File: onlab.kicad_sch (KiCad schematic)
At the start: 82 parts, among them J1 Battery, J10 DC-Motor, J2 HC_SR04, J3 HC_SR04, J4 HC_SR04, J5 DC-Motor, J6 DC-Motor, J7 DC-Motor, J8 DC-Motor, J9 DC-Motor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

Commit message: Routing
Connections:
- net Mot2_DrvA: now also U5.13 (P12/GPIO12/ADC2_CH5); no longer U5.25 (P0/GPIO0/ADC2_CH1)
- net Mot2_DrvB: now also U5.15 (P13/GPIO13/ADC2_CH4); no longer U5.24 (P2/GPIO2/ADC_CH2)
- net Mot3_DrvA: now also U5.25 (P0/GPIO0/ADC2_CH1); no longer U5.13 (P12/GPIO12/ADC2_CH5)
- net Mot3_DrvB: now also U5.24 (P2/GPIO2/ADC_CH2); no longer U5.15 (P13/GPIO13/ADC2_CH4)
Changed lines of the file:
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@@
     (effects (font (size 1.27 1.27)) (justify right bottom))
   )
-  (label "Mot2_DrvA" (at 254 69.85 0) (fields_autoplaced)
+  (label "Mot3_DrvA" (at 254 69.85 0) (fields_autoplaced)
     (effects (font (size 1.27 1.27)) (justify left bottom))
   )
@@
     (effects (font (size 1.27 1.27)) (justify left bottom))
   )
-  (label "Mot2_DrvB" (at 254 72.39 0) (fields_autoplaced)
+  (label "Mot3_DrvB" (at 254 72.39 0) (fields_autoplaced)
     (effects (font (size 1.27 1.27)) (justify left bottom))
   )
@@
     (effects (font (size 1.27 1.27)) (justify left bottom))
   )
-  (label "Mot3_DrvA" (at 190.5 67.31 180) (fields_autoplaced)
+  (label "Mot2_DrvA" (at 190.5 67.31 180) (fields_autoplaced)
     (effects (font (size 1.27 1.27)) (justify right bottom))
   )
@@
     (effects (font (size 1.27 1.27)) (justify left bottom))
   )
-  (label "Mot3_DrvB" (at 190.5 72.39 180) (fields_autoplaced)
+  (label "Mot2_DrvB" (at 190.5 72.39 180) (fields_autoplaced)
     (effects (font (size 1.27 1.27)) (justify right bottom))
   )

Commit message: Routing part 2
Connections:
- net Mot1_DrvA: now also U5.10 (P26/GPIO26/ADC2_CH9); no longer U5.9 (P25/GPIO25/ADC2_CH8)
- net Mot1_DrvB: now also U5.9 (P25/GPIO25/ADC2_CH8); no longer U5.10 (P26/GPIO26/ADC2_CH9)
- net Mot1_EncA: now also U5.3 (SVP/GPIO36/ADC1_CH0); no longer U5.5 (P34/GPIO34/ADC1_CH6)
- net Mot1_EncB: now also U5.4 (SVN/GPIO39/ADC1_CH3); no longer U5.6 (P35/GPIO35/ADC1_CH7)
- net Mot2_DrvA: now also U5.8 (P33/GPIO33/ADC1_CH5); no longer U5.13 (P12/GPIO12/ADC2_CH5)
- net Mot2_DrvB: now also U5.7 (P32/GPIO32/ADC1_CH4); no longer U5.15 (P13/GPIO13/ADC2_CH4)
- net Mot2_EncA: now also U5.5 (P34/GPIO34/ADC1_CH6); no longer U5.7 (P32/GPIO32/ADC1_CH4)
- net Mot2_EncB: now also U5.6 (P35/GPIO35/ADC1_CH7); no longer U5.8 (P33/GPIO33/ADC1_CH5)
- net Mot3_EncA: now also U5.13 (P12/GPIO12/ADC2_CH5); no longer U5.3 (SVP/GPIO36/ADC1_CH0)
- net Mot3_EncB: now also U5.15 (P13/GPIO13/ADC2_CH4); no longer U5.4 (SVN/GPIO39/ADC1_CH3)
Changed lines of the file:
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@@
+    (effects (font (size 1.27 1.27)) (justify right bottom))
+  )
+  (label "Mot2_EncB" (at 190.5 49.53 180) (fields_autoplaced)
     (effects (font (size 1.27 1.27)) (justify right bottom))
   )
@@
     (effects (font (size 1.27 1.27)) (justify left bottom))
   )
+  (label "Mot1_EncB" (at 190.5 44.45 180) (fields_autoplaced)
+    (effects (font (size 1.27 1.27)) (justify right bottom))
+  )
   (label "UV_Trig_1" (at 44.45 248.92 180) (fields_autoplaced)
     (effects (font (size 1.27 1.27)) (justify right bottom))
@@
     (effects (font (size 1.27 1.27)) (justify right bottom))
   )
-  (label "Mot3_EncA" (at 190.5 41.91 180) (fields_autoplaced)
+  (label "Mot2_EncA" (at 190.5 46.99 180) (fields_autoplaced)
+    (effects (font (size 1.27 1.27)) (justify right bottom))
+  )
+  (label "Mot2_DrvB" (at 190.5 52.07 180) (fields_autoplaced)
     (effects (font (size 1.27 1.27)) (justify right bottom))
   )
@@
     (effects (font (size 1.27 1.27)) (justify right bottom))
   )
+  (label "Mot3_EncA" (at 190.5 67.31 180) (fields_autoplaced)
+    (effects (font (size 1.27 1.27)) (justify right bottom))
+  )
   (label "Mot3_A" (at 369.062 72.644 0) (fields_autoplaced)
     (effects (font (size 1.27 1.27)) (justify left bottom))
@@
     (effects (font (size 1.27 1.27)) (justify right bottom))
   )
+  (label "Mot1_DrvB" (at 190.5 57.15 180) (fields_autoplaced)
+    (effects (font (size 1.27 1.27)) (justify right bottom))
+  )
   (label "Mot2_DrvA" (at 351.282 49.784 180) (fields_autoplaced)
     (effects (font (size 1.27 1.27)) (justify right bottom))
@@
     (effects (font (size 1.27 1.27)) (justify right bottom))
   )
+  (label "Mot3_EncB" (at 190.5 72.39 180) (fields_autoplaced)
+    (effects (font (size 1.27 1.27)) (justify right bottom))
+  )
+  (label "Mot1_DrvA" (at 190.5 59.69 180) (fields_autoplaced)
+    (effects (font (size 1.27 1.27)) (justify right bottom))
+  )
   (label "Mot3_EncA" (at 352.425 234.95 180) (fields_autoplaced)
     (effects (font (size 1.27 1.27)) (justify right bottom))
@@
     (effects (font (size 1.27 1.27)) (justify left bottom))
   )
-  (label "Mot3_EncB" (at 190.5 44.45 180) (fields_autoplaced)
-    (effects (font (size 1.27 1.27)) (justify right bottom))
-  )
   (label "Mot3_A" (at 352.425 229.87 180) (fields_autoplaced)
     (effects (font (size 1.27 1.27)) (justify right bottom))
@@
     (effects (font (size 1.27 1.27)) (justify left bottom))
   )
+  (label "Mot2_DrvA" (at 190.5 54.61 180) (fields_autoplaced)
+    (effects (font (size 1.27 1.27)) (justify right bottom))
+  )
   (label "Mot1_EncB" (at 349.885 140.97 180) (fields_autoplaced)
     (effects (font (size 1.27 1.27)) (justify right bottom))
@@
     (effects (font (size 1.27 1.27)) (justify left bottom))
   )
-  (label "Mot2_EncB" (at 190.5 54.61 180) (fields_autoplaced)
-    (effects (font (size 1.27 1.27)) (justify right bottom))
-  )
   (label "Mot1_DrvB" (at 351.282 42.164 180) (fields_autoplaced)
     (effects (font (size 1.27 1.27)) (justify right bottom))
@@
     (effects (font (size 1.27 1.27)) (justify left bottom))
   )
-  (label "Mot2_DrvA" (at 190.5 67.31 180) (fields_autoplaced)
-    (effects (font (size 1.27 1.27)) (justify right bottom))
-  )
   (label "SCLK" (at 106.426 82.296 0) (fields_autoplaced)
     (effects (font (size 1.27 1.27)) (justify left bottom))
@@
     (effects (font (size 1.27 1.27)) (justify left bottom))
   )
-  (label "Mot2_DrvB" (at 190.5 72.39 180) (fields_autoplaced)
-    (effects (font (size 1.27 1.27)) (justify right bottom))
-  )
-  (label "Mot1_EncB" (at 190.5 49.53 180) (fields_autoplaced)
-    (effects (font (size 1.27 1.27)) (justify right bottom))
-  )
   (label "MPU95 interrupt" (at 266.954 83.312 0) (fields_autoplaced)
     (effects (font (size 1.27 1.27)) (justify left bottom))
@@
     (effects (font (size 1.27 1.27)) (justify left bottom))
   )
-  (label "Mot1_DrvA" (at 190.5 57.15 180) (fields_autoplaced)
-    (effects (font (size 1.27 1.27)) (justify right bottom))
-  )
   (label "Button_2" (at 207.01 129.54 180) (fields_autoplaced)
     (effects (font (size 1.27 1.27)) (justify right bottom))
@@
     (effects (font (size 1.27 1.27)) (justify left bottom))
   )
-  (label "Mot1_EncA" (at 190.5 46.99 180) (fields_autoplaced)
-    (effects (font (size 1.27 1.27)) (justify right bottom))
-  )
   (label "Mot2_DrvB" (at 351.282 52.324 180) (fields_autoplaced)
     (effects (font (size 1.27 1.27)) (justify right bottom))
@@
     (effects (font (size 1.27 1.27)) (justify right bottom))
   )
+  (label "Mot1_EncA" (at 190.5 41.91 180) (fields_autoplaced)
+    (effects (font (size 1.27 1.27)) (justify right bottom))
+  )
   (label "I2C_SDA" (at 42.418 136.398 180) (fields_autoplaced)
     (effects (font (size 1.27 1.27)) (justify right bottom))
@@
     (effects (font (size 1.27 1.27)) (justify right bottom))
   )
-  (label "Mot1_DrvB" (at 190.5 59.69 180) (fields_autoplaced)
-    (effects (font (size 1.27 1.27)) (justify right bottom))
-  )
   (label "nCS" (at 254 59.69 0) (fields_autoplaced)
     (effects (font (size 1.27 1.27)) (justify left bottom))
@@
     (effects (font (size 1.27 1.27)) (justify right bottom))
   )
-  (label "Mot2_EncA" (at 190.5 52.07 180) (fields_autoplaced)
-    (effects (font (size 1.27 1.27)) (justify right bottom))
-  )

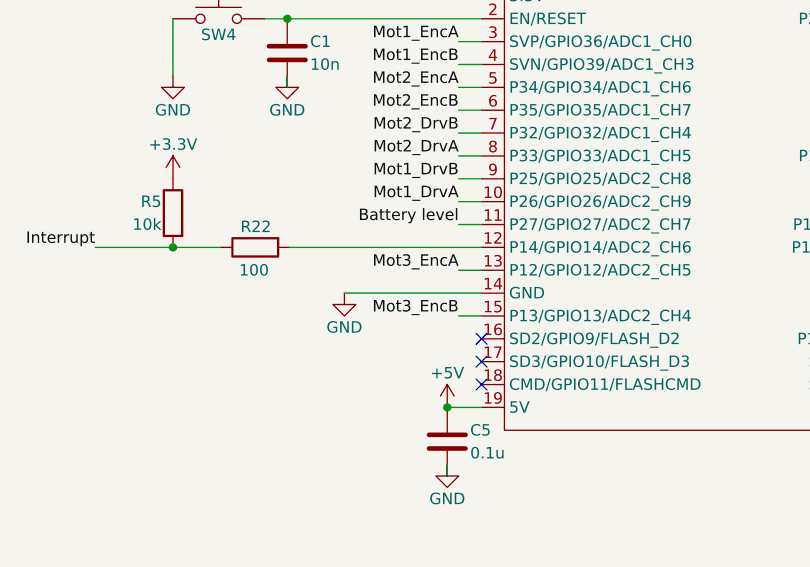
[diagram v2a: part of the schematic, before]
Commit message: Routing part 3 - remain to be done motors and vcc
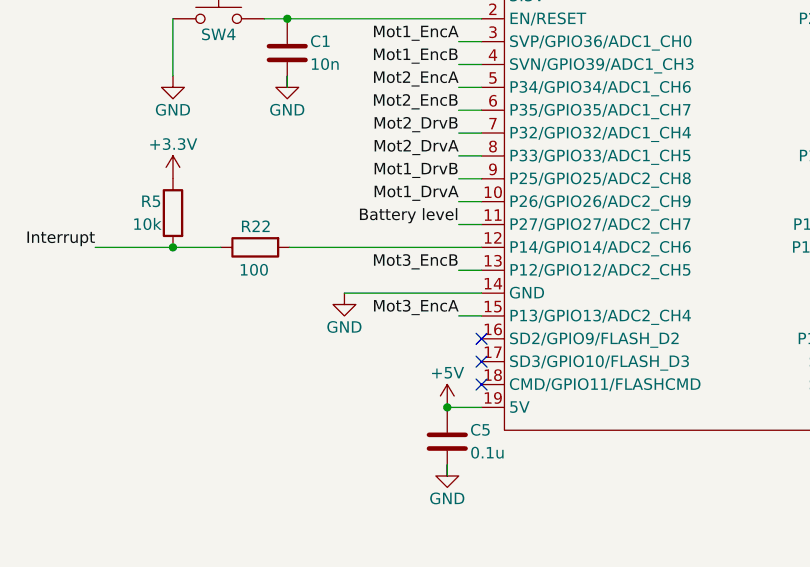
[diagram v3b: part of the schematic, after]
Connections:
- net Mot3_EncA: now also U5.15 (P13/GPIO13/ADC2_CH4); no longer U5.13 (P12/GPIO12/ADC2_CH5)
- net Mot3_EncB: now also U5.13 (P12/GPIO12/ADC2_CH5); no longer U5.15 (P13/GPIO13/ADC2_CH4)
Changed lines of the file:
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@@
-    (effects (font (size 1.27 1.27)) (justify right bottom))
-  )
-  (label "Mot3_EncA" (at 190.5 67.31 180) (fields_autoplaced)
     (effects (font (size 1.27 1.27)) (justify right bottom))
   )
@@
     (effects (font (size 1.27 1.27)) (justify right bottom))
   )
-  (label "Mot3_EncB" (at 190.5 72.39 180) (fields_autoplaced)
+  (label "Mot3_EncA" (at 190.5 72.39 180) (fields_autoplaced)
     (effects (font (size 1.27 1.27)) (justify right bottom))
   )
@@
     (effects (font (size 1.27 1.27)) (justify right bottom))
   )
+  (label "Mot3_EncB" (at 190.5 67.31 180) (fields_autoplaced)
+    (effects (font (size 1.27 1.27)) (justify right bottom))
+  )

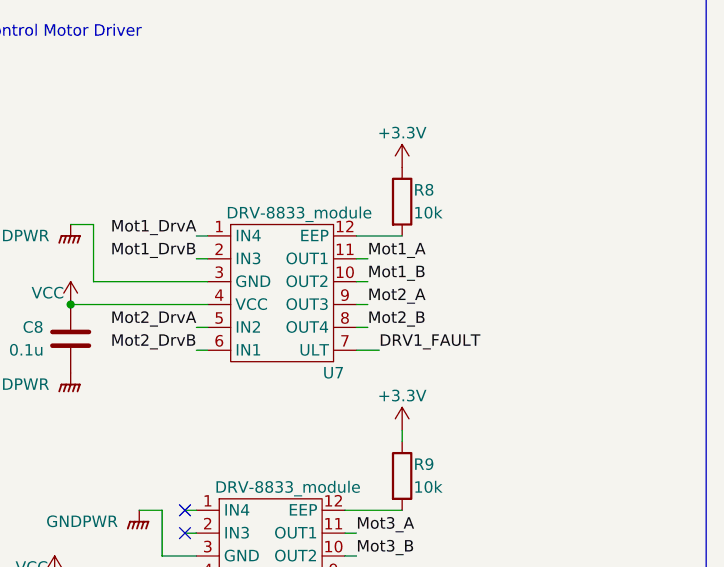
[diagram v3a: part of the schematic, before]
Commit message: Routing part 4 - remain to be done GND and GNDPWR
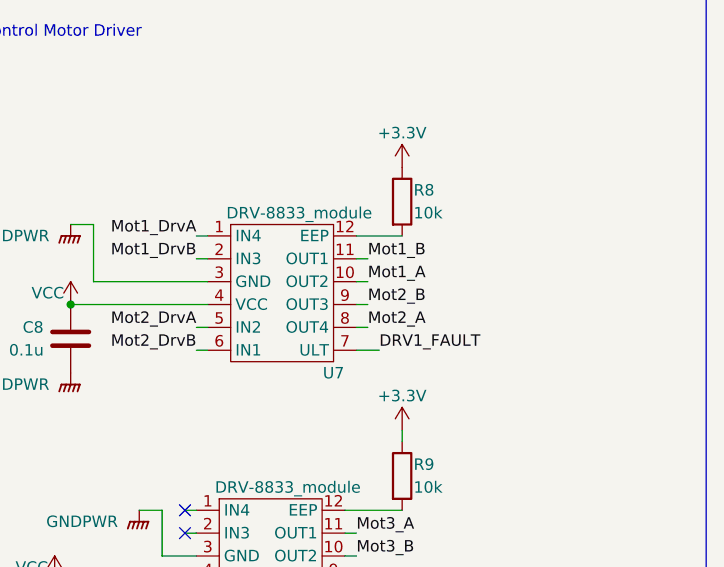
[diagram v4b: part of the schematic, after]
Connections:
- net Mot1_A: now also U7.10 (OUT2); no longer U7.11 (OUT1)
- net Mot1_B: now also U7.11 (OUT1); no longer U7.10 (OUT2)
- net Mot2_A: now also U7.8 (OUT4); no longer U7.9 (OUT3)
- net Mot2_B: now also U7.9 (OUT3); no longer U7.8 (OUT4)
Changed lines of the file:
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@@
     (effects (font (size 1.27 1.27)) (justify right bottom))
-  )
-  (label "Mot2_B" (at 370.332 49.784 0) (fields_autoplaced)
-    (effects (font (size 1.27 1.27)) (justify left bottom))
   )
   (label "UV_Echo_2" (at 254 64.77 0) (fields_autoplaced)
@@
   (label "LED_1" (at 206.502 178.054 180) (fields_autoplaced)
     (effects (font (size 1.27 1.27)) (justify right bottom))
+  )
+  (label "Mot1_A" (at 370.332 44.704 0) (fields_autoplaced)
+    (effects (font (size 1.27 1.27)) (justify left bottom))
   )
   (label "Mot3_A" (at 369.062 72.644 0) (fields_autoplaced)
@@
   (label "Battery level" (at 190.5 62.23 180) (fields_autoplaced)
     (effects (font (size 1.27 1.27)) (justify right bottom))
+  )
+  (label "Mot2_B" (at 370.332 47.244 0) (fields_autoplaced)
+    (effects (font (size 1.27 1.27)) (justify left bottom))
   )
   (label "Mot3_EncA" (at 190.5 72.39 180) (fields_autoplaced)
@@
     (effects (font (size 1.27 1.27)) (justify left bottom))
   )
-  (label "Mot1_A" (at 370.332 42.164 0) (fields_autoplaced)
-    (effects (font (size 1.27 1.27)) (justify left bottom))
-  )
   (label "Mot1_DrvA" (at 351.282 39.624 180) (fields_autoplaced)
     (effects (font (size 1.27 1.27)) (justify right bottom))
@@
   (label "Mot3_DrvB" (at 350.012 82.804 180) (fields_autoplaced)
     (effects (font (size 1.27 1.27)) (justify right bottom))
-  )
-  (label "Mot1_B" (at 370.332 44.704 0) (fields_autoplaced)
-    (effects (font (size 1.27 1.27)) (justify left bottom))
   )
   (label "SCLK" (at 106.426 82.296 0) (fields_autoplaced)
@@
     (effects (font (size 1.27 1.27)) (justify right bottom))
   )
+  (label "Mot2_A" (at 370.332 49.784 0) (fields_autoplaced)
+    (effects (font (size 1.27 1.27)) (justify left bottom))
+  )
   (label "LED_Heart" (at 267.208 66.294 0) (fields_autoplaced)
     (effects (font (size 1.27 1.27)) (justify left bottom))
@@
     (effects (font (size 1.27 1.27)) (justify right bottom))
   )
-  (label "Mot2_A" (at 370.332 47.244 0) (fields_autoplaced)
+  (label "Mot1_B" (at 370.332 42.164 0) (fields_autoplaced)
     (effects (font (size 1.27 1.27)) (justify left bottom))
   )
